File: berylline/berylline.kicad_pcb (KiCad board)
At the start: 2 copper layers, 97.6 x 80.8 mm, 28 parts, among them J1 Val**, J2 Battery_Cell, J3 Battery_Cell

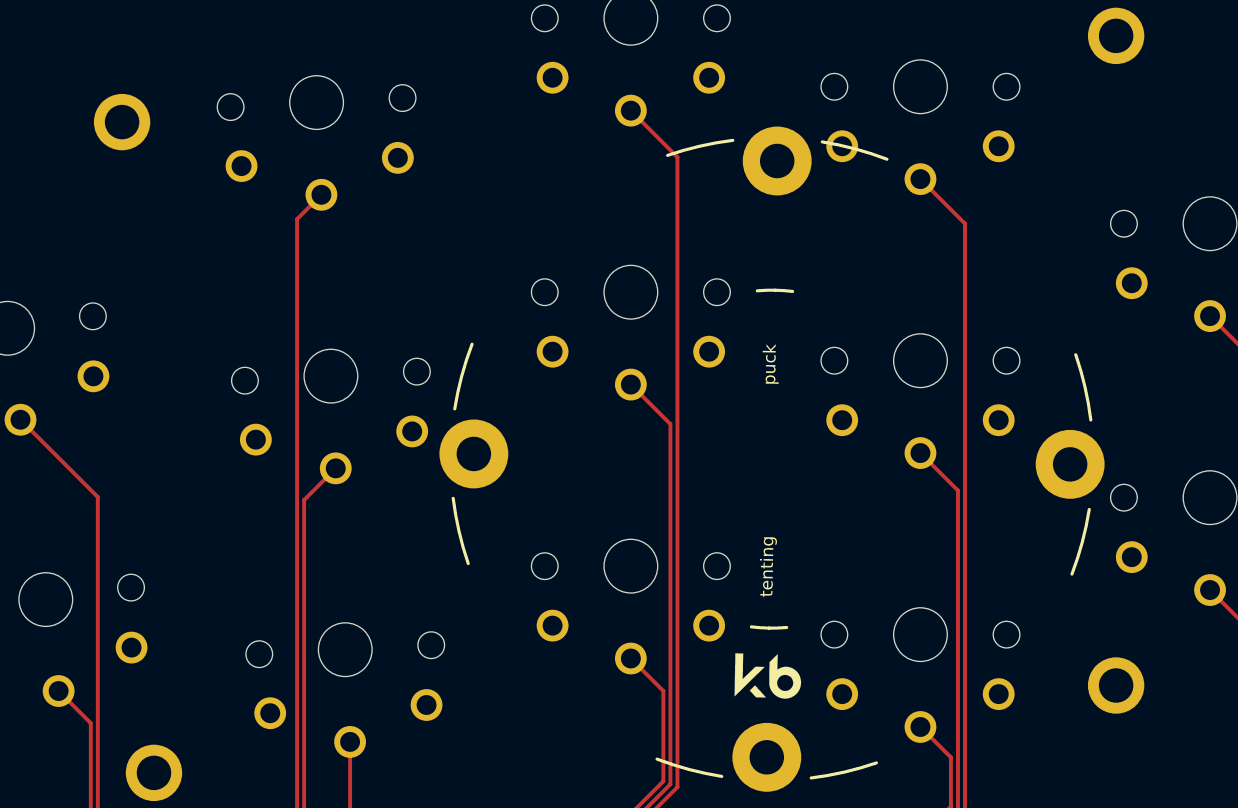
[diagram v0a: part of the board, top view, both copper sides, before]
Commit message: Remove a couple of case mounts
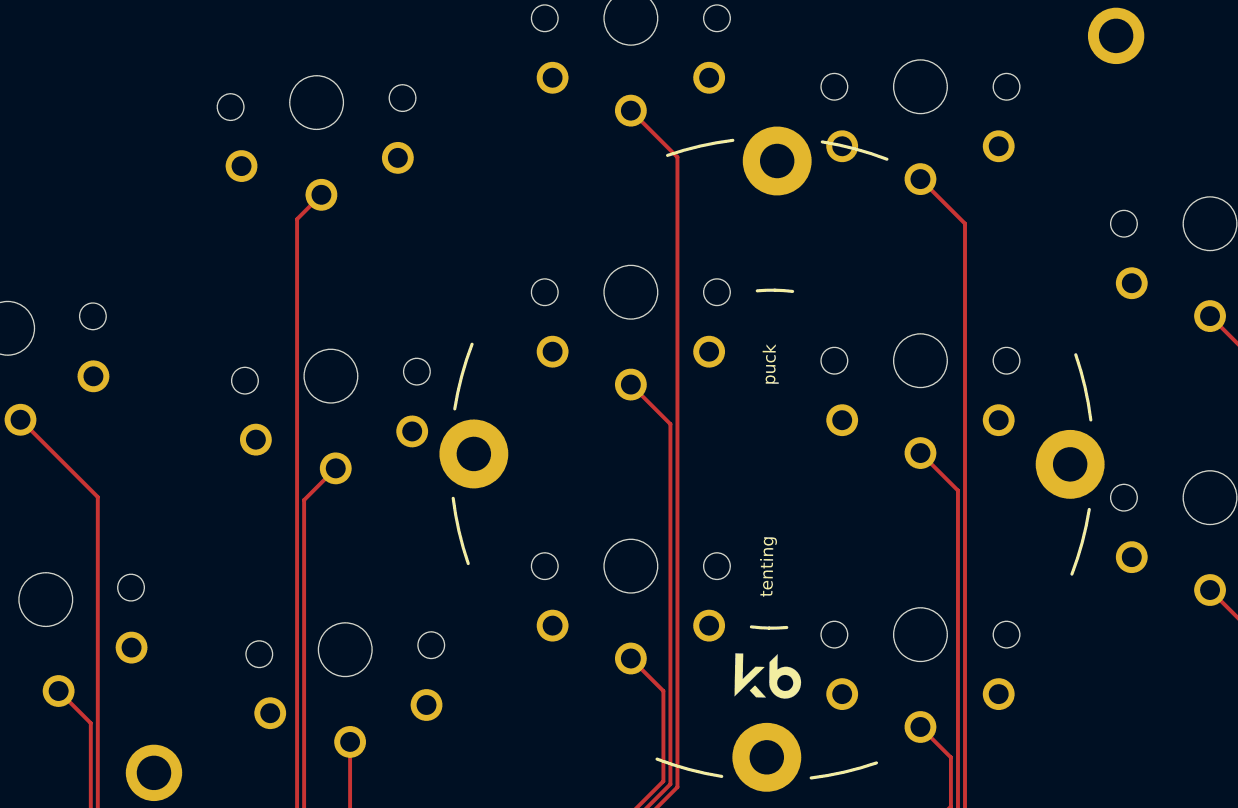
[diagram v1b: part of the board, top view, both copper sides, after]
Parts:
- removed the ? at (186.1, 138.3)
- removed the ? at (249.6, 174.2)
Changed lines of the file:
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@@
       (outputformat 1)
       (mirror false)
-      (drillshape 1)
+      (drillshape 0)
       (scaleselection 1)
-      (outputdirectory "")
+      (outputdirectory "gerbers")
     )
   )
@@
       (net 11 "P8"))
   )
-  (footprint "" (layer "F.Cu")
-    (at 186.071176 138.257272)
-    (fp_text reference "" (at 0 0) (layer "F.SilkS")
-      (effects (font (size 1.27 1.27) (thickness 0.15)))
-    )
-    (fp_text value "" (at 0 0) (layer "F.SilkS")
-      (effects (font (size 1.27 1.27) (thickness 0.15)))
-    )
-    (pad "1" thru_hole circle (at 0 0 358) (size 3.6 3.6) (drill 2.2) (layers *.Cu *.Mask))
-  )
   (footprint "trochilidae:PG1350Reversible" (layer "F.Cu")
     (at 198.496084 137.010186 -177)
@@
       (net 6 "P14"))
   )
-  (footprint "trochilidae:M2MountingHoleSlimSimple" (layer "F.Cu")
-    (at 249.573519 174.25 -8)
-    (fp_text reference "" (at 0 -3.2 14) (layer "F.SilkS") hide
-      (effects (font (size 1 1) (thickness 0.15)))
-    )
-    (fp_text value "Val**" (at 0 0 172) (layer "F.SilkS") hide
-      (effects (font (size 1.27 1.27) (thickness 0.15)))
-    )
-    (fp_circle (center 0 0) (end 2 0) (layer "F.CrtYd") (width 0.05) (fill none))
-    (pad "1" thru_hole circle (at 0 0 14) (size 3.6 3.6) (drill 2.2) (layers *.Cu *.Mask))
-  )
   (footprint "trochilidae:PG1350Reversible" (layer "F.Cu")
